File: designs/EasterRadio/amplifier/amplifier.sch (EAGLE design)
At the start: 14 parts, among them IC1 PAM8403DR, J1 STX-3120-3BM, J2 S2B-NSHSS-TB, J3 S2B-NSHSS-TB

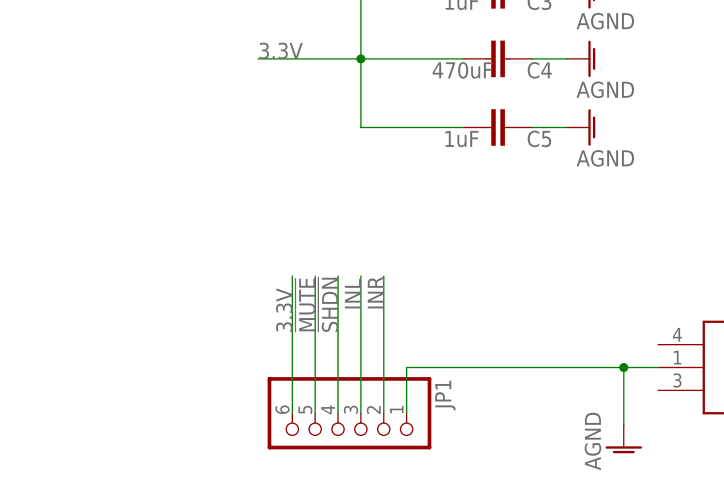
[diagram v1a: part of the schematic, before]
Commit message: added amplifier brd
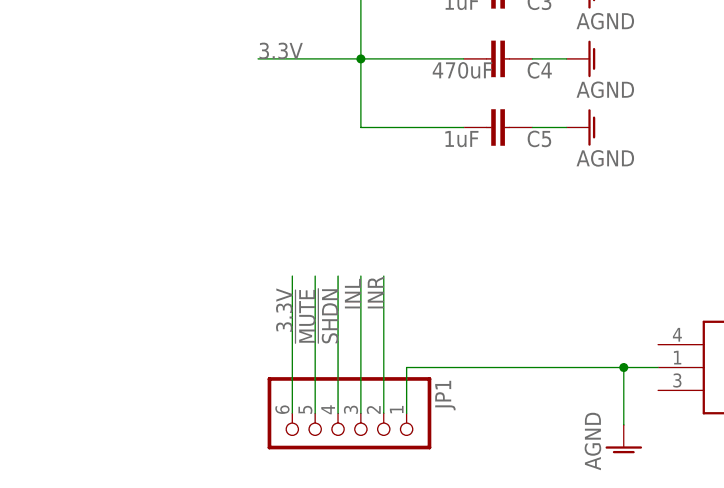
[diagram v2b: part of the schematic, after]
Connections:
- removed net N$15: JP1.5
- removed net N$16: JP1.4
- net !MUTE: now also JP1.5
- net !SHDN: now also JP1.4
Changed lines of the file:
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@@
 </segment>
 <segment>
-<label x="33.02" y="21.59" size="1.778" layer="95" rot="R90"/>
+<pinref part="JP1" gate="A" pin="5"/>
+<wire x1="33.02" y1="12.7" x2="33.02" y2="27.94" width="0.1524" layer="91"/>
+<label x="33.02" y="20.32" size="1.778" layer="95" rot="R90"/>
 </segment>
 </net>
@@
 </segment>
 <segment>
-<label x="35.56" y="21.59" size="1.778" layer="95" rot="R90"/>
+<pinref part="JP1" gate="A" pin="4"/>
+<wire x1="35.56" y1="12.7" x2="35.56" y2="27.94" width="0.1524" layer="91"/>
+<label x="35.56" y="20.32" size="1.778" layer="95" rot="R90"/>
 </segment>
 </net>
@@
 </segment>
 </net>
-<net name="N$15" class="0">
-<segment>
-<pinref part="JP1" gate="A" pin="5"/>
-<wire x1="33.02" y1="12.7" x2="33.02" y2="27.94" width="0.1524" layer="91"/>
-</segment>
-</net>
-<net name="N$16" class="0">
-<segment>
-<pinref part="JP1" gate="A" pin="4"/>
-<wire x1="35.56" y1="12.7" x2="35.56" y2="27.94" width="0.1524" layer="91"/>
-</segment>
-</net>

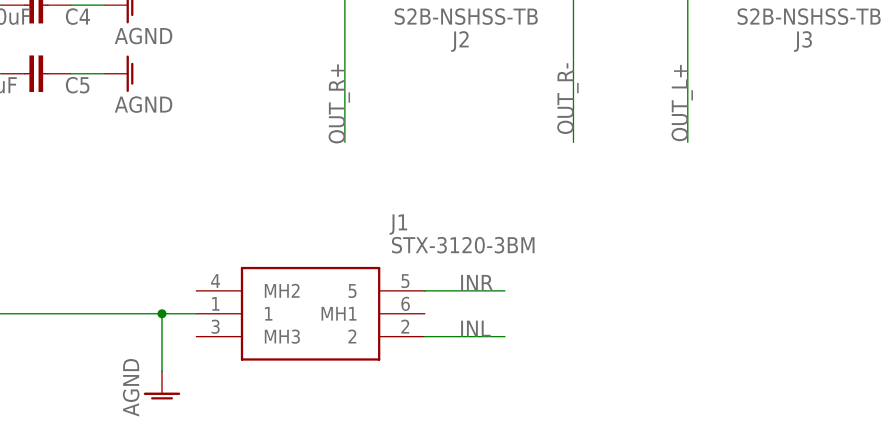
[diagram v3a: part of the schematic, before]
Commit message: added mainboard layout and new 3.5mm jack
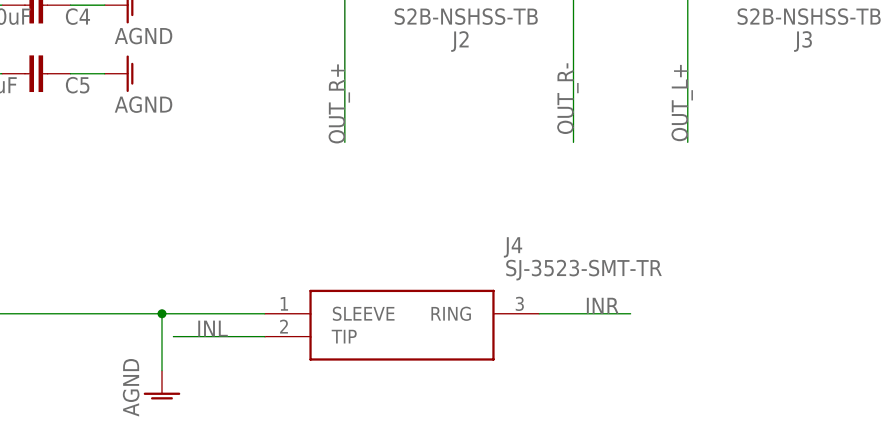
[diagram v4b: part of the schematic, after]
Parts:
- removed J1: STX-3120-3BM, MouserUseful:STX-3120-3BM
- added J4: SJ-3523-SMT-TR, MouserUseful:SJ-3523-SMT-TR
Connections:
- removed net N$17: JP1.3
- removed net N$18: JP1.2
- net AGND: now also J4.SLEEVE; no longer J1.1
- net INL: now also J4.TIP, JP1.3; no longer J1.2
- net INR: now also J4.RING, JP1.2; no longer J1.5
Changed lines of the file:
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@@
 <part name="AGND15" library="supply1" library_urn="urn:adsk.eagle:library:371" deviceset="AGND" device=""/>
 <part name="AGND16" library="supply1" library_urn="urn:adsk.eagle:library:371" deviceset="AGND" device=""/>
-<part name="J1" library="MouserUseful" deviceset="STX-3120-3BM" device=""/>
 <part name="AGND17" library="supply1" library_urn="urn:adsk.eagle:library:371" deviceset="AGND" device=""/>
 <part name="J2" library="CommonParts" deviceset="S2B-NSHSS-TB" device=""/>
 <part name="J3" library="CommonParts" deviceset="S2B-NSHSS-TB" device=""/>
 <part name="JP1" library="pinhead" library_urn="urn:adsk.eagle:library:325" deviceset="PINHD-1X6" device="" package3d_urn="urn:adsk.eagle:package:22472/2"/>
+<part name="J4" library="MouserUseful" deviceset="SJ-3523-SMT-TR" device=""/>
 </parts>
 <sheets>
@@
 <attribute name="VALUE" x="68.58" y="41.91" size="1.778" layer="96" rot="R180"/>
 </instance>
-<instance part="J1" gate="G$1" x="71.12" y="20.32" smashed="yes">
-<attribute name="NAME" x="92.71" y="27.94" size="1.778" layer="95" align="center-left"/>
-<attribute name="VALUE" x="92.71" y="25.4" size="1.778" layer="96" align="center-left"/>
-</instance>
 <instance part="AGND17" gate="VR1" x="67.31" y="8.89" smashed="yes">
 <attribute name="VALUE" x="64.77" y="6.35" size="1.778" layer="96" rot="R90"/>
@@
 <attribute name="NAME" x="46.355" y="16.51" size="1.778" layer="95" rot="R270"/>
 <attribute name="VALUE" x="25.4" y="16.51" size="1.778" layer="96" rot="R270"/>
+</instance>
+<instance part="J4" gate="G$1" x="78.74" y="17.78" smashed="yes">
+<attribute name="NAME" x="105.41" y="25.4" size="1.778" layer="95" align="center-left"/>
+<attribute name="VALUE" x="105.41" y="22.86" size="1.778" layer="96" align="center-left"/>
 </instance>
 </instances>
@@
 </segment>
 <segment>
-<pinref part="J1" gate="G$1" pin="1"/>
 <pinref part="AGND17" gate="VR1" pin="AGND"/>
-<wire x1="71.12" y1="17.78" x2="67.31" y2="17.78" width="0.1524" layer="91"/>
 <wire x1="67.31" y1="17.78" x2="67.31" y2="11.43" width="0.1524" layer="91"/>
 <pinref part="JP1" gate="A" pin="1"/>
@@
 <wire x1="43.18" y1="17.78" x2="67.31" y2="17.78" width="0.1524" layer="91"/>
 <junction x="67.31" y="17.78"/>
+<pinref part="J4" gate="G$1" pin="SLEEVE"/>
+<wire x1="78.74" y1="17.78" x2="67.31" y2="17.78" width="0.1524" layer="91"/>
 </segment>
 </net>
@@
 </segment>
 <segment>
-<pinref part="J1" gate="G$1" pin="5"/>
-<wire x1="96.52" y1="20.32" x2="105.41" y2="20.32" width="0.1524" layer="91"/>
-<label x="100.33" y="20.32" size="1.778" layer="95"/>
-</segment>
-<segment>
 <label x="40.64" y="24.13" size="1.778" layer="95" rot="R90"/>
+</segment>
+<segment>
+<pinref part="J4" gate="G$1" pin="RING"/>
+<wire x1="109.22" y1="17.78" x2="119.38" y2="17.78" width="0.1524" layer="91"/>
+<label x="114.3" y="17.78" size="1.778" layer="95"/>
+</segment>
+<segment>
+<pinref part="JP1" gate="A" pin="2"/>
+<wire x1="40.64" y1="12.7" x2="40.64" y2="27.94" width="0.1524" layer="91"/>
 </segment>
 </net>
@@
 </segment>
 <segment>
-<pinref part="J1" gate="G$1" pin="2"/>
-<wire x1="96.52" y1="15.24" x2="105.41" y2="15.24" width="0.1524" layer="91"/>
-<label x="100.33" y="15.24" size="1.778" layer="95"/>
-</segment>
-<segment>
 <label x="38.1" y="24.13" size="1.778" layer="95" rot="R90"/>
+</segment>
+<segment>
+<pinref part="J4" gate="G$1" pin="TIP"/>
+<wire x1="78.74" y1="15.24" x2="68.58" y2="15.24" width="0.1524" layer="91"/>
+<label x="71.12" y="15.24" size="1.778" layer="95"/>
+</segment>
+<segment>
+<pinref part="JP1" gate="A" pin="3"/>
+<wire x1="38.1" y1="12.7" x2="38.1" y2="27.94" width="0.1524" layer="91"/>
 </segment>
 </net>
@@
 </segment>
 </net>
-<net name="N$17" class="0">
-<segment>
-<pinref part="JP1" gate="A" pin="3"/>
-<wire x1="38.1" y1="12.7" x2="38.1" y2="27.94" width="0.1524" layer="91"/>
-</segment>
-</net>
-<net name="N$18" class="0">
-<segment>
-<pinref part="JP1" gate="A" pin="2"/>
-<wire x1="40.64" y1="12.7" x2="40.64" y2="27.94" width="0.1524" layer="91"/>
-</segment>
-</net>

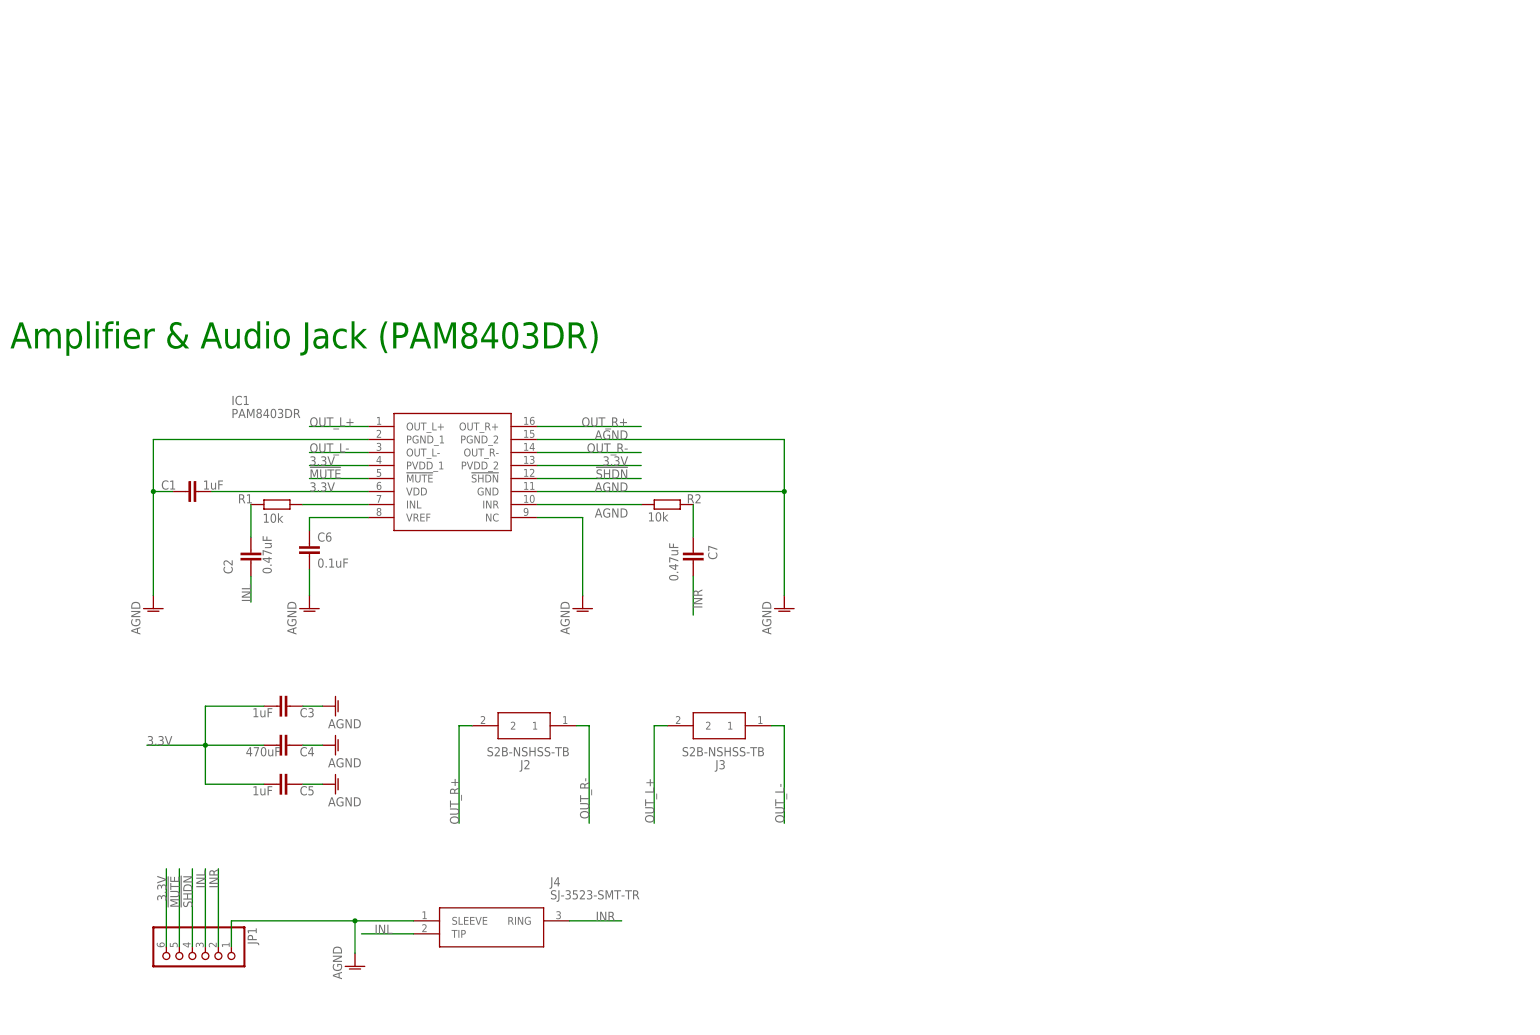
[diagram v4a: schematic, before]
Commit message: changes for new design excluding swap for amplifier
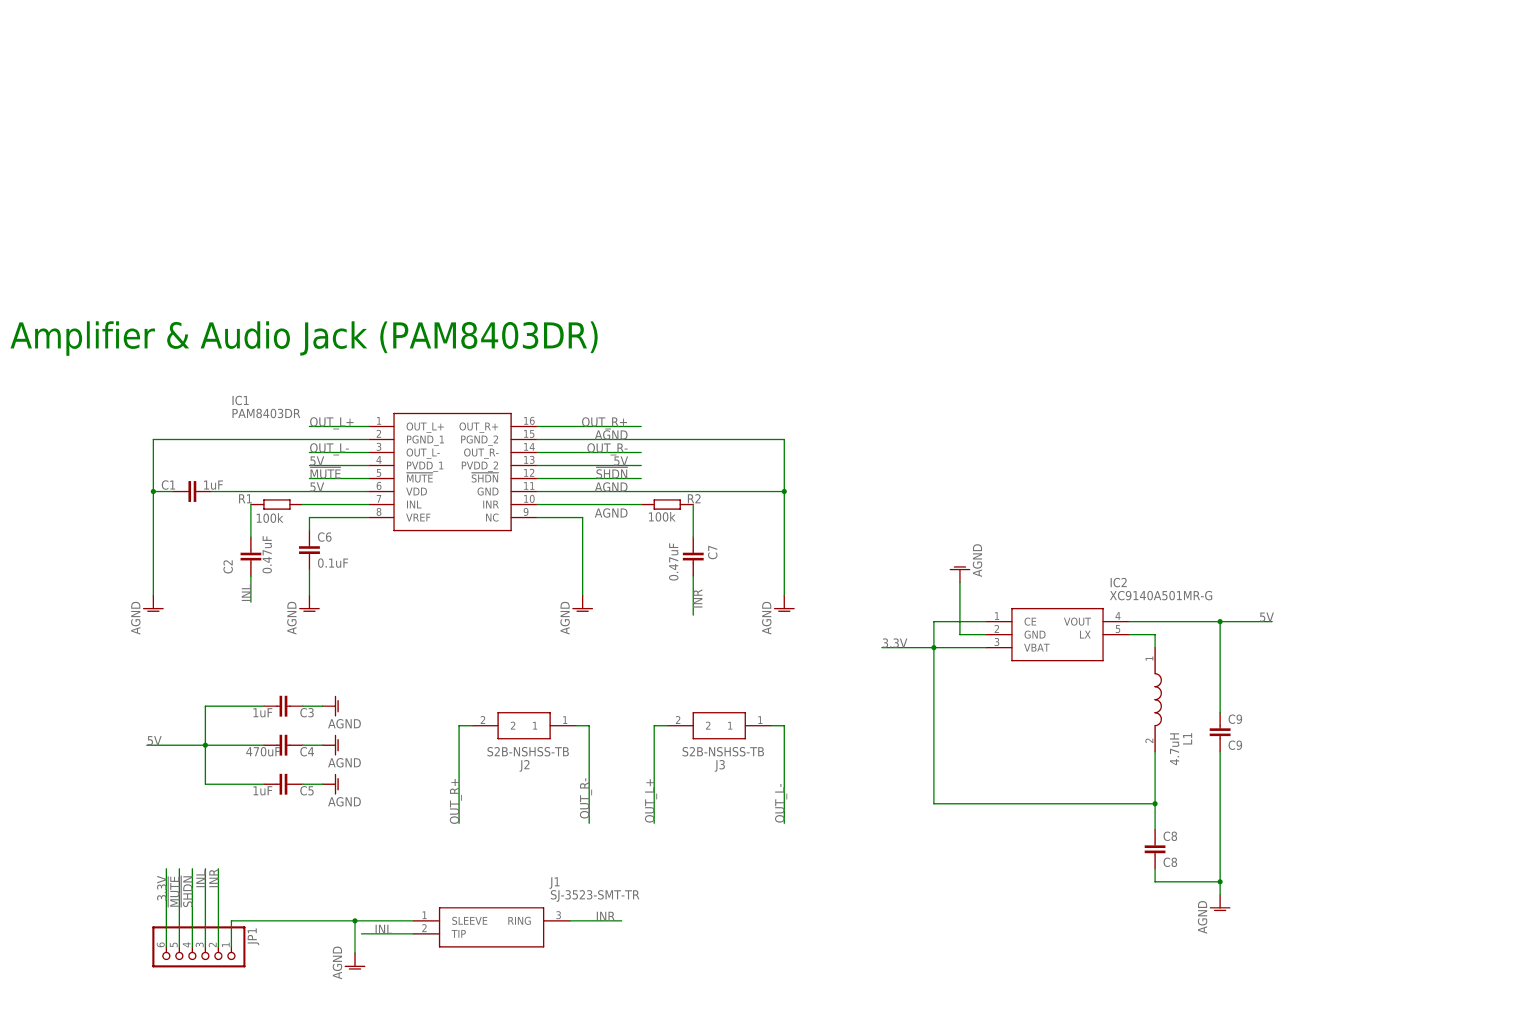
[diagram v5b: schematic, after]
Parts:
- added C8: C8, rcl:C-EUC1206K
- added C9: C9, rcl:C-EUC1206K
- added IC2: XC9140A501MR-G, MouserUseful:XC9140A501MR-G
- added L1: 4.7uH, MouserUseful:VLS6045EX-221M
- R1, R2: value 10k -> 100k
- renumbered J4 to J1
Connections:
- new net 5V: C1.1, C3.1, C4.1, C5.1, C9.1, IC1.PVDD_1, IC1.PVDD_2, IC1.VDD, IC2.VOUT
- new net N$1: IC2.LX, L1.1
- net 3.3V: now also C8.1, IC2.CE, IC2.VBAT, L1.2; no longer C1.1, C3.1, C4.1, C5.1, IC1.PVDD_1, IC1.PVDD_2, IC1.VDD
- net AGND: now also C8.2, C9.2, IC2.GND

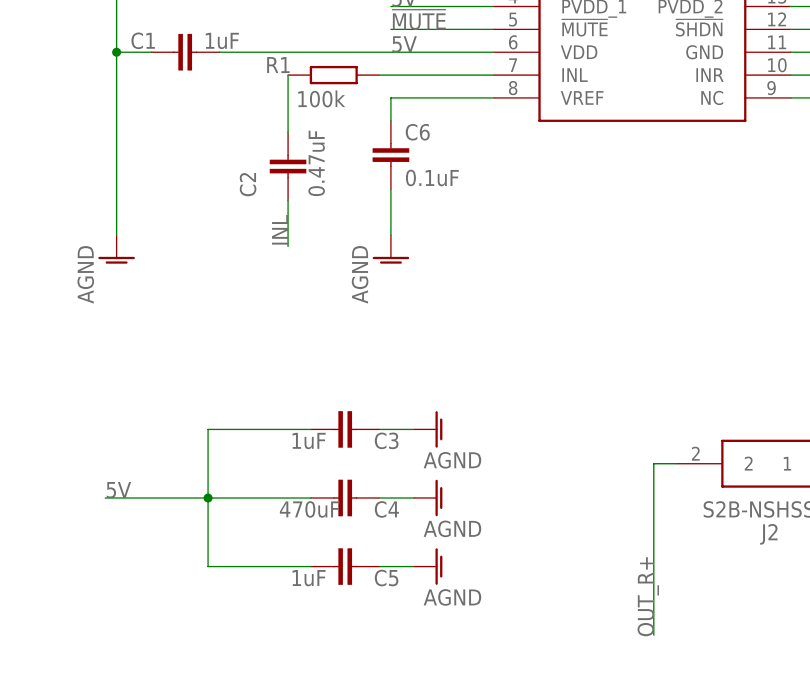
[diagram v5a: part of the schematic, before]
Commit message: changed mainboard design radio
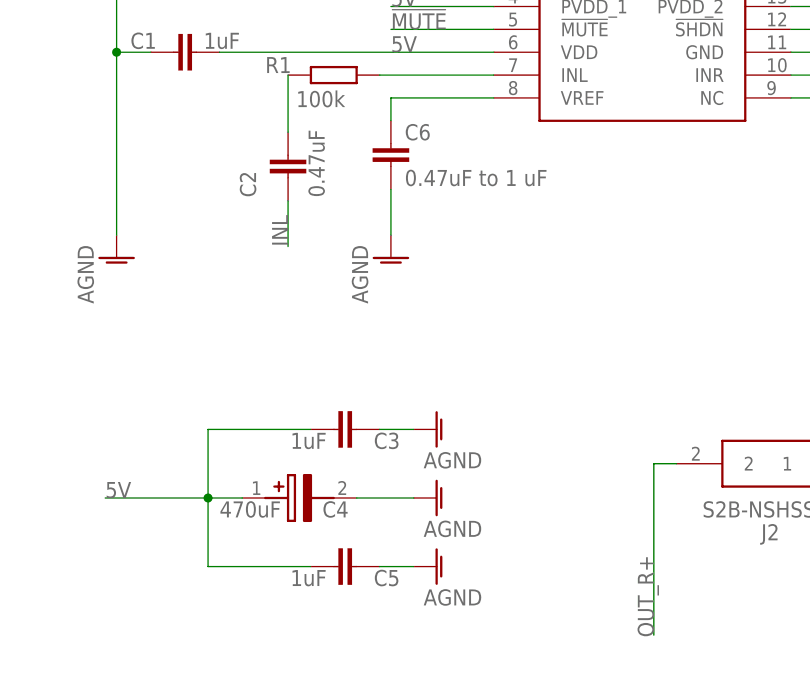
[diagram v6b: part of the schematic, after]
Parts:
- C4: device CommonParts:C-EU_805C0805 -> MouserUseful:293D477X9010E2TE3
- C6: value 0.1uF -> 0.47uF to 1 uF
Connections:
- net 5V: now also C4.+; no longer C4.1
- net AGND: now also C4.-; no longer C4.2
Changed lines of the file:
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@@
 <setting verticaltext="up"/>
 </settings>
-<grid distance="0.1" unitdist="inch" unit="inch" style="lines" multiple="1" display="no" altdistance="0.01" altunitdist="inch" altunit="inch"/>
+<grid distance="0.05" unitdist="inch" unit="inch" style="lines" multiple="1" display="no" altdistance="0.01" altunitdist="inch" altunit="inch"/>
 <layers>
 <layer number="1" name="Top" color="4" fill="1" visible="no" active="no"/>
@@
 <part name="R1" library="CommonParts" deviceset="R-EU_805" device="R0805" package3d_urn="urn:adsk.eagle:package:23553/2" value="100k"/>
 <part name="C2" library="CommonParts" deviceset="C-EU_805" device="C0805" package3d_urn="urn:adsk.eagle:package:23617/2" value="0.47uF"/>
-<part name="C6" library="CommonParts" deviceset="C-EU_805" device="C0805" package3d_urn="urn:adsk.eagle:package:23617/2" value="0.1uF"/>
+<part name="C6" library="CommonParts" deviceset="C-EU_805" device="C0805" package3d_urn="urn:adsk.eagle:package:23617/2" value="0.47uF to 1 uF"/>
 <part name="AGND12" library="supply1" library_urn="urn:adsk.eagle:library:371" deviceset="AGND" device=""/>
 <part name="C1" library="CommonParts" deviceset="C-EU_805" device="C0805" package3d_urn="urn:adsk.eagle:package:23617/2" value="1uF"/>
@@
 <part name="C7" library="CommonParts" deviceset="C-EU_805" device="C0805" package3d_urn="urn:adsk.eagle:package:23617/2" value="0.47uF"/>
 <part name="AGND13" library="supply1" library_urn="urn:adsk.eagle:library:371" deviceset="AGND" device=""/>
-<part name="C4" library="CommonParts" deviceset="C-EU_805" device="C0805" package3d_urn="urn:adsk.eagle:package:23617/2" value="470uF"/>
 <part name="C3" library="CommonParts" deviceset="C-EU_805" device="C0805" package3d_urn="urn:adsk.eagle:package:23617/2" value="1uF"/>
 <part name="C5" library="CommonParts" deviceset="C-EU_805" device="C0805" package3d_urn="urn:adsk.eagle:package:23617/2" value="1uF"/>
@@
 <part name="AGND2" library="supply1" library_urn="urn:adsk.eagle:library:371" deviceset="AGND" device=""/>
 <part name="AGND3" library="supply1" library_urn="urn:adsk.eagle:library:371" deviceset="AGND" device=""/>
+<part name="C4" library="MouserUseful" deviceset="293D477X9010E2TE3" device="" value="470uF"/>
 </parts>
 <sheets>
@@
 <attribute name="VALUE" x="109.22" y="73.66" size="1.778" layer="96" rot="R90"/>
 </instance>
-<instance part="C4" gate="G$1" x="52.07" y="52.07" smashed="yes" rot="R90">
-<attribute name="NAME" x="59.436" y="51.689" size="1.778" layer="95" rot="R180"/>
-<attribute name="VALUE" x="45.974" y="49.911" size="1.778" layer="96"/>
-</instance>
 <instance part="C3" gate="G$1" x="52.07" y="59.69" smashed="yes" rot="R90">
 <attribute name="NAME" x="59.436" y="59.309" size="1.778" layer="95" rot="R180"/>
@@
 <instance part="AGND3" gate="VR1" x="185.42" y="86.36" smashed="yes" rot="R180">
 <attribute name="VALUE" x="187.96" y="91.44" size="1.778" layer="96" rot="R270"/>
+</instance>
+<instance part="C4" gate="G$1" x="41.91" y="52.07" smashed="yes">
+<attribute name="NAME" x="50.8" y="50.8" size="1.778" layer="95" align="center-left"/>
+<attribute name="VALUE" x="39.37" y="50.8" size="1.778" layer="96" align="center-left"/>
 </instance>
 </instances>
@@
 <segment>
 <pinref part="AGND15" gate="VR1" pin="AGND"/>
-<pinref part="C4" gate="G$1" pin="2"/>
-<wire x1="60.96" y1="52.07" x2="57.15" y2="52.07" width="0.1524" layer="91"/>
+<wire x1="60.96" y1="52.07" x2="54.61" y2="52.07" width="0.1524" layer="91"/>
+<pinref part="C4" gate="G$1" pin="-"/>
 </segment>
 <segment>
@@
 </segment>
 <segment>
-<pinref part="C4" gate="G$1" pin="1"/>
 <wire x1="26.67" y1="52.07" x2="38.1" y2="52.07" width="0.1524" layer="91"/>
-<wire x1="38.1" y1="52.07" x2="49.53" y2="52.07" width="0.1524" layer="91"/>
 <wire x1="38.1" y1="59.69" x2="49.53" y2="59.69" width="0.1524" layer="91"/>
 <pinref part="C3" gate="G$1" pin="1"/>
@@
 <wire x1="38.1" y1="52.07" x2="38.1" y2="44.45" width="0.1524" layer="91"/>
 <junction x="38.1" y="52.07"/>
-</segment>
-<segment>
+<pinref part="C4" gate="G$1" pin="+"/>
+<wire x1="38.1" y1="52.07" x2="41.91" y2="52.07" width="0.1524" layer="91"/>
+</segment>
+<segment>
